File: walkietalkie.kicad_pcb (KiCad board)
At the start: 2 copper layers, 51.2 x 89.7 mm, 10 parts, among them J1 Conn_01x05_Pin, SW1 PTT, U2 NRF24L01_Breakout, U7 ER_OLEDM0.91_1x-I2C

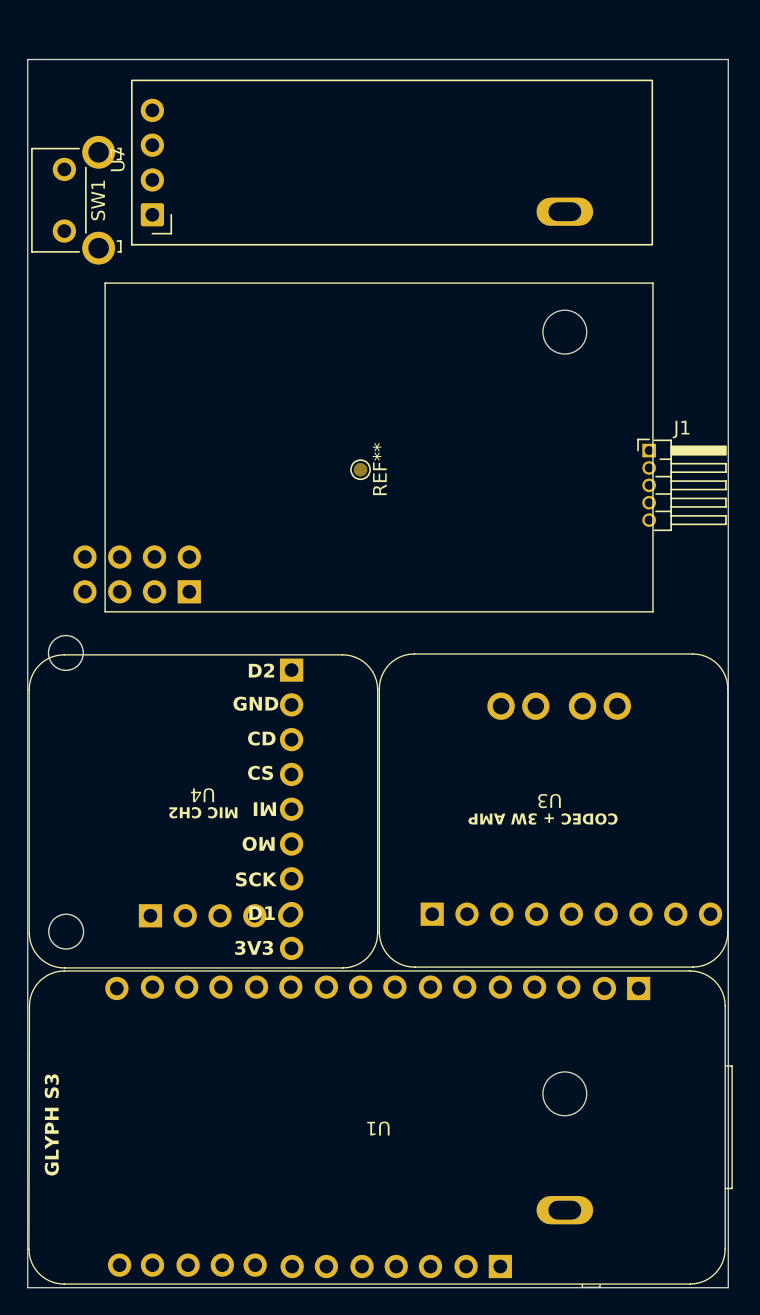
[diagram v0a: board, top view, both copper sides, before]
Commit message: feat: finalize component placement, routing remaining
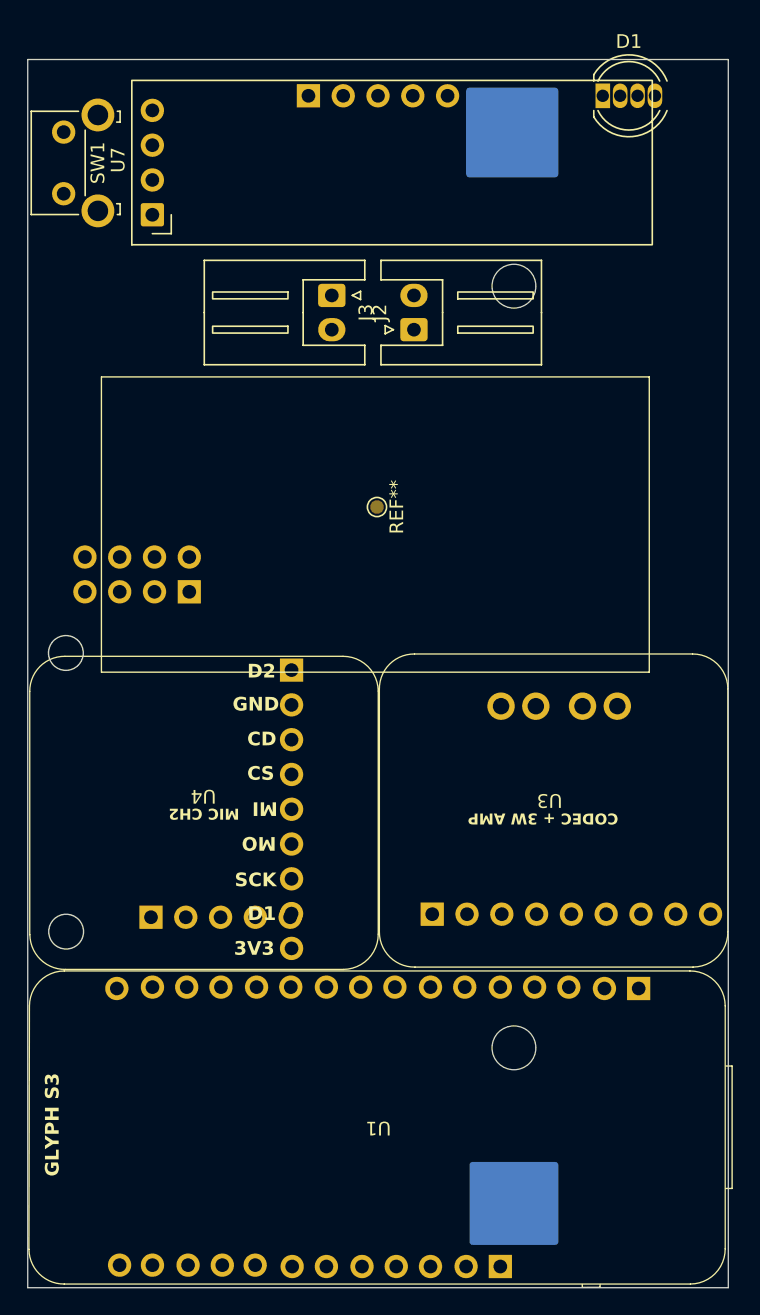
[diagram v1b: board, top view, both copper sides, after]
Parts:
- added D1: LED_KRGB, LED_THT:LED_D5.0mm-4_RGB, F.Cu at (156.5, 63.0)
- added J2: Conn_01x02_Pin, Connector_JST:JST_XH_S2B-XH-A_1x02_P2.50mm_Horizontal, F.Cu at (136.7, 77.5)
- added J3: Conn_01x02_Pin, Connector_JST:JST_XH_S2B-XH-A_1x02_P2.50mm_Horizontal, F.Cu at (142.7, 80.0)
- BT1: footprint pcbcupid_footprint:BAT_BK-18650-PC2 -> pcbcupidd_footprint:BatteryHolder_1042_1x18650
- J1: footprint Connector_PinHeader_1.27mm:PinHeader_1x05_P1.27mm_Horizontal -> Connector_PinHeader_2.54mm:PinHeader_1x05_P2.54mm_Vertical; moved to B.Cu
- moved J1 35.9 mm to (135.0, 63.0), turned to -90 degrees
- moved BT1 4.88 mm to (150.0, 104.9)
- moved REF** 2.98 mm to (140.0, 93.0)
- moved SW1 2.73 mm to (117.1, 70.1)
- moved U4 0.11 mm to (127.4, 115.5)
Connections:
- U1 pad 27: unconnected-(U1-TX-Pad27) -> Net-(U1-TX)
- U5 pad 3: unconnected-(U5-SCK-Pad3) -> /SCK
- U5 pad 4: unconnected-(U5-MO-Pad4) -> /MO
- U5 pad 5: unconnected-(U5-MI-Pad5) -> /MI
- U5 pad 6: unconnected-(U5-CS-Pad6) -> Net-(U1-TX)

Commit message: feat: initial routing progress, fix 2ch mic footprint
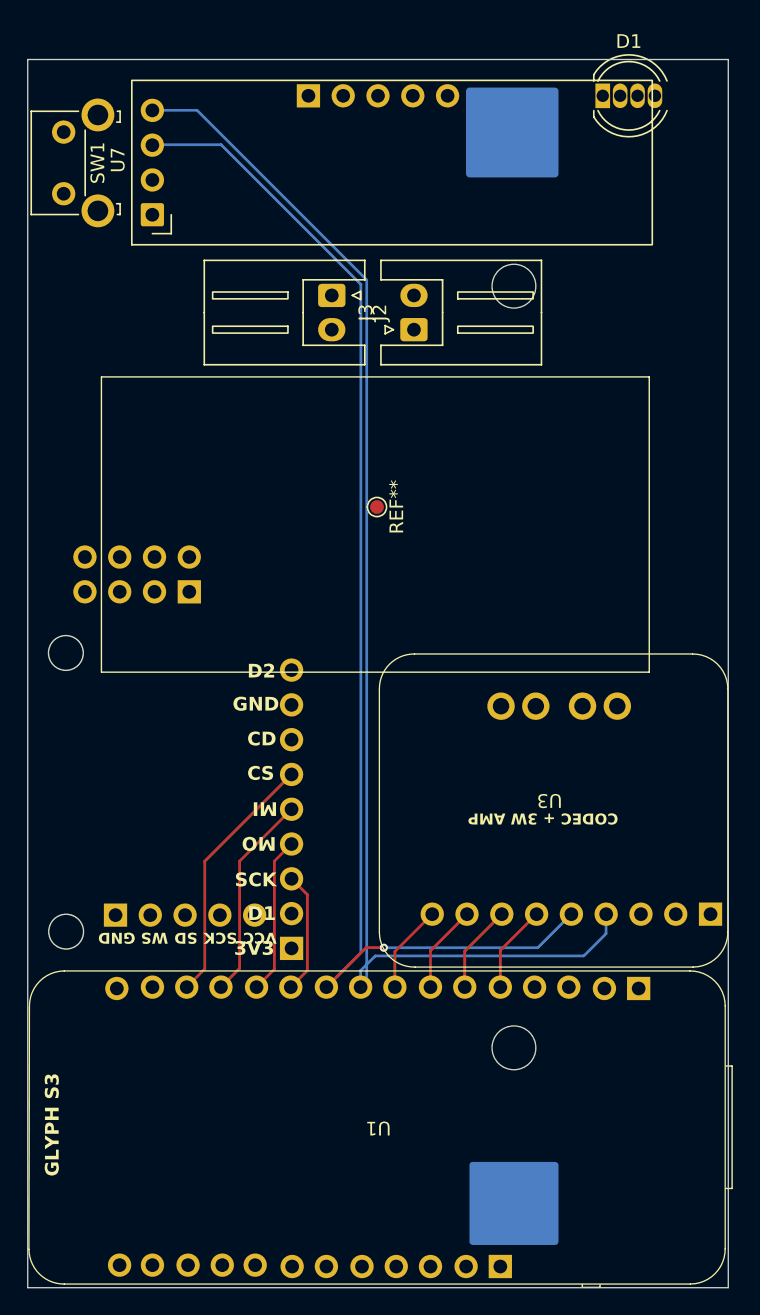
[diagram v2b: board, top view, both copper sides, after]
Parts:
- U4: footprint pcbcupid_footprint:gsense-microphone_2ch -> pcbcupidd_footprint:CH2 mic; moved to B.Cu
- moved U4 1.30 mm to (128.2, 114.5), turned to 0 degrees
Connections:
- U1 pad 1: /SCL -> unconnected-(U1-SCL-Pad1)
- U1 pad 17: /CE -> /NAU_MCLK
- U1 pad 18: /CSN -> /BCLK
- U1 pad 19: unconnected-(U1-D15-Pad19) -> /NAU_DAT
- U1 pad 2: /SDA -> unconnected-(U1-SDA-Pad2)
- U1 pad 20: /MIC_SD -> /LRCK
- U1 pad 21: /LRCK -> /SDA
- U1 pad 22: /BCLK -> /SCL
- U1 pad 26: unconnected-(U1-RX-Pad26) -> Net-(U1-RX)
- U1 pad 27: Net-(U1-TX) -> /MIC_SD
- U1 pad 5: /NAU_MCLK -> unconnected-(U1-A6-Pad5)
- U1 pad 6: /NAU_DAT -> unconnected-(U1-A7-Pad6)
- U5 pad 6: Net-(U1-TX) -> Net-(U1-RX)
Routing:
- net /SDA: track 0.00 -> 94.3 mm
- net /SCL: track 0.00 -> 92.3 mm, vias 0 -> 1
- net Net-(U1-RX): track 0.00 -> 18.7 mm
- net /MI: track 0.00 -> 15.1 mm
- net /MO: track 0.00 -> 11.5 mm
- net /SCK: track 0.00 -> 8.88 mm
- net /LRCK: track 0.00 -> 6.45 mm
- net /BCLK: track 0.00 -> 6.45 mm
- net /NAU_DAT: track 0.00 -> 6.43 mm
- net /NAU_MCLK: track 0.00 -> 6.42 mm

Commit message: feat: routing almost done, GND and VCC remaining
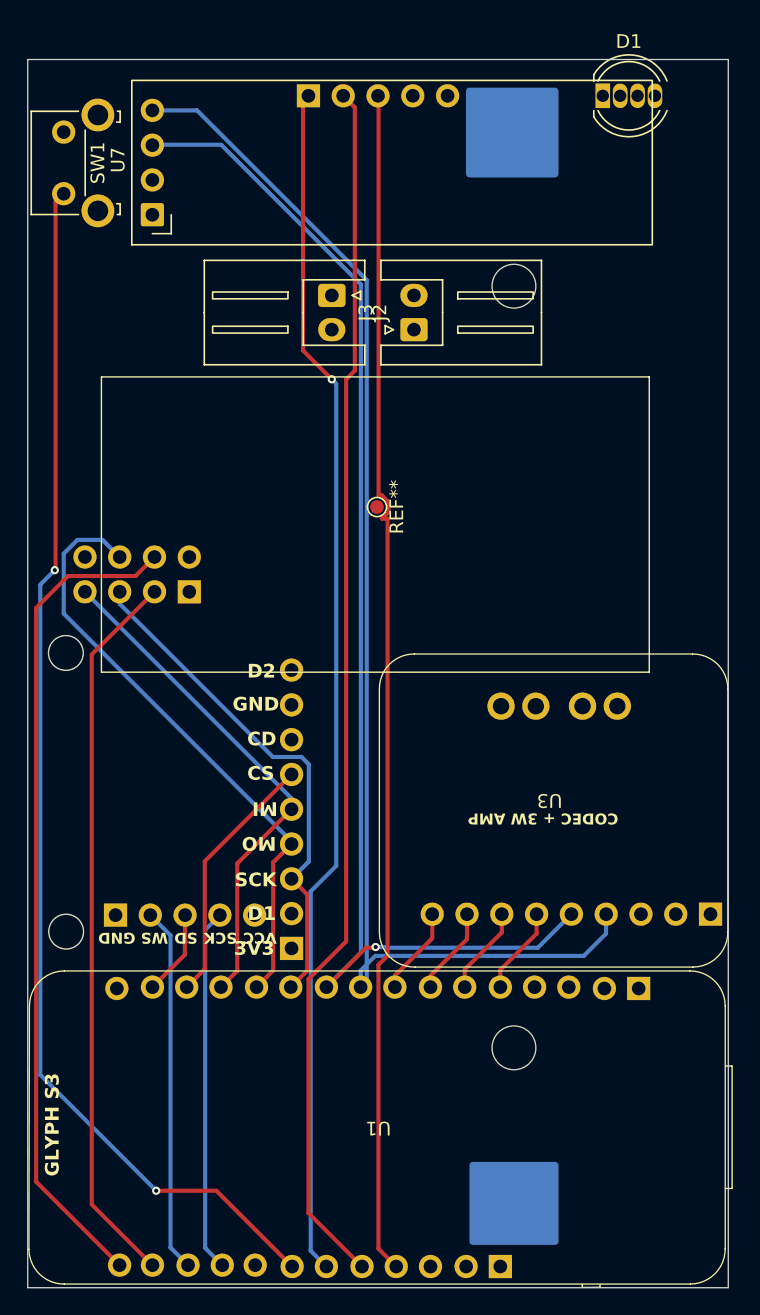
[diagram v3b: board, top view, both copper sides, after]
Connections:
- U1 pad 1: unconnected-(U1-SCL-Pad1) -> /CSN
- U1 pad 2: unconnected-(U1-SDA-Pad2) -> /CE
- U1 pad 3: unconnected-(U1-A1-Pad3) -> /WS
- U1 pad 4: /ENC_SW -> /MSCK
- U1 pad 6: unconnected-(U1-A7-Pad6) -> /PTT
- U1 pad 8: /PTT -> /ENC_B
- U1 pad 9: /ENC_B -> /ENC_SW
- U4 pad 1: +3.3V -> GND
- U4 pad 2: GND -> /WS
- U4 pad 3: /LRCK -> /MIC_SD
- U4 pad 4: /BCLK -> /MSCK
- U4 pad 5: /MIC_SD -> +3.3V
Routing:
- net /PTT: track 0.00 -> 89.2 mm, vias 0 -> 2
- net /ENC_B: track 0.00 -> 88.8 mm
- net /ENC_A: track 0.00 -> 87.9 mm, vias 0 -> 1
- net /ENC_SW: track 0.00 -> 87.4 mm
- net /CSN: track 0.00 -> 60.7 mm
- net /CE: track 0.00 -> 52.9 mm
- net /MO: track 11.5 -> 44.6 mm
- net /SCK: track 8.88 -> 37.3 mm
- net /WS: track 0.00 -> 26.7 mm
- net /MSCK: track 0.00 -> 26.5 mm
- net /MI: track 15.1 -> 37.2 mm
- net /MIC_SD: track 0.00 -> 6.27 mm
